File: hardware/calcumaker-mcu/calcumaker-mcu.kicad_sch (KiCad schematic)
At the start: 0 parts

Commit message: Checkpoint
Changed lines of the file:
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@@
 	)
 	(sheet
-		(at 320.04 40.64)
-		(size 36 22)
-		(exclude_from_sim no)
-		(in_bom yes)
-		(on_board yes)
-		(dnp no)
+		(at 40.64 40.64)
+		(size 36.00 22.00)
 		(fields_autoplaced yes)
-		(stroke
-			(width 0.1524)
-			(type solid)
+		(stroke (width 0.1524) (type solid))
+		(fill (color 0 0 0 0.0000))
+		(property "Sheetname" "MCU"
+			(at 40.64 39.37 0)
+			(effects (font (size 1.27 1.27)) (justify left bottom))
 		)
-		(fill
-			(color 0 0 0 0)
-		)
-		(property "Sheetname" "KeyboardIF"
-			(at 320.04 39.37 0)
-			(show_name no)
-			(do_not_autoplace no)
-			(effects
-				(font
-					(size 1.27 1.27)
-				)
-				(justify left bottom)
-			)
-		)
-		(property "Sheetfile" "keyboard_if.kicad_sch"
-			(at 320.04 63.91 0)
-			(show_name no)
-			(do_not_autoplace no)
-			(effects
-				(font
-					(size 1.27 1.27)
-				)
-				(justify left top)
-			)
+		(property "Sheetfile" "mcu.kicad_sch"
+			(at 40.64 63.91 0)
+			(effects (font (size 1.27 1.27)) (justify left top))
 		)
 	)
 	(sheet
-		(at 40.64 40.64)
-		(size 36 22)
-		(exclude_from_sim no)
-		(in_bom yes)
-		(on_board yes)
-		(dnp no)
+		(at 96.52 40.64)
+		(size 36.00 22.00)
 		(fields_autoplaced yes)
-		(stroke
-			(width 0.1524)
-			(type solid)
+		(stroke (width 0.1524) (type solid))
+		(fill (color 0 0 0 0.0000))
+		(property "Sheetname" "PSU"
+			(at 96.52 39.37 0)
+			(effects (font (size 1.27 1.27)) (justify left bottom))
 		)
-		(fill
-			(color 0 0 0 0)
-		)
-		(property "Sheetname" "MCU"
-			(at 40.64 39.37 0)
-			(show_name no)
-			(do_not_autoplace no)
-			(effects
-				(font
-					(size 1.27 1.27)
-				)
-				(justify left bottom)
-			)
-		)
-		(property "Sheetfile" "mcu.kicad_sch"
-			(at 40.64 63.91 0)
-			(show_name no)
-			(do_not_autoplace no)
-			(effects
-				(font
-					(size 1.27 1.27)
-				)
-				(justify left top)
-			)
+		(property "Sheetfile" "psu.kicad_sch"
+			(at 96.52 63.91 0)
+			(effects (font (size 1.27 1.27)) (justify left top))
 		)
 	)
 	(sheet
-		(at 375.92 40.64)
-		(size 36 22)
-		(exclude_from_sim no)
-		(in_bom yes)
-		(on_board yes)
-		(dnp no)
+		(at 152.40 40.64)
+		(size 36.00 22.00)
 		(fields_autoplaced yes)
-		(stroke
-			(width 0.1524)
-			(type solid)
+		(stroke (width 0.1524) (type solid))
+		(fill (color 0 0 0 0.0000))
+		(property "Sheetname" "KeyboardIF"
+			(at 152.40 39.37 0)
+			(effects (font (size 1.27 1.27)) (justify left bottom))
 		)
-		(fill
-			(color 0 0 0 0)
-		)
-		(property "Sheetname" "QSPIFlash"
-			(at 375.92 39.37 0)
-			(show_name no)
-			(do_not_autoplace no)
-			(effects
-				(font
-					(size 1.27 1.27)
-				)
-				(justify left bottom)
-			)
-		)
-		(property "Sheetfile" "qspi_flash.kicad_sch"
-			(at 375.92 63.91 0)
-			(show_name no)
-			(do_not_autoplace no)
-			(effects
-				(font
-					(size 1.27 1.27)
-				)
-				(justify left top)
-			)
+		(property "Sheetfile" "keyboard_if.kicad_sch"
+			(at 152.40 63.91 0)
+			(effects (font (size 1.27 1.27)) (justify left top))
 		)
 	)
 	(sheet
 		(at 208.28 40.64)
-		(size 36 22)
-		(exclude_from_sim no)
-		(in_bom yes)
-		(on_board yes)
-		(dnp no)
+		(size 36.00 22.00)
 		(fields_autoplaced yes)
-		(stroke
-			(width 0.1524)
-			(type solid)
+		(stroke (width 0.1524) (type solid))
+		(fill (color 0 0 0 0.0000))
+		(property "Sheetname" "QSPIFlash"
+			(at 208.28 39.37 0)
+			(effects (font (size 1.27 1.27)) (justify left bottom))
 		)
-		(fill
-			(color 0 0 0 0)
-		)
-		(property "Sheetname" "PSU"
-			(at 208.28 39.37 0)
-			(show_name no)
-			(do_not_autoplace no)
-			(effects
-				(font
-					(size 1.27 1.27)
-				)
-				(justify left bottom)
-			)
-		)
-		(property "Sheetfile" "psu.kicad_sch"
+		(property "Sheetfile" "qspi_flash.kicad_sch"
 			(at 208.28 63.91 0)
-			(show_name no)
-			(do_not_autoplace no)
-			(effects
-				(font
-					(size 1.27 1.27)
-				)
-				(justify left top)
-			)
+			(effects (font (size 1.27 1.27)) (justify left top))
 		)
 	)

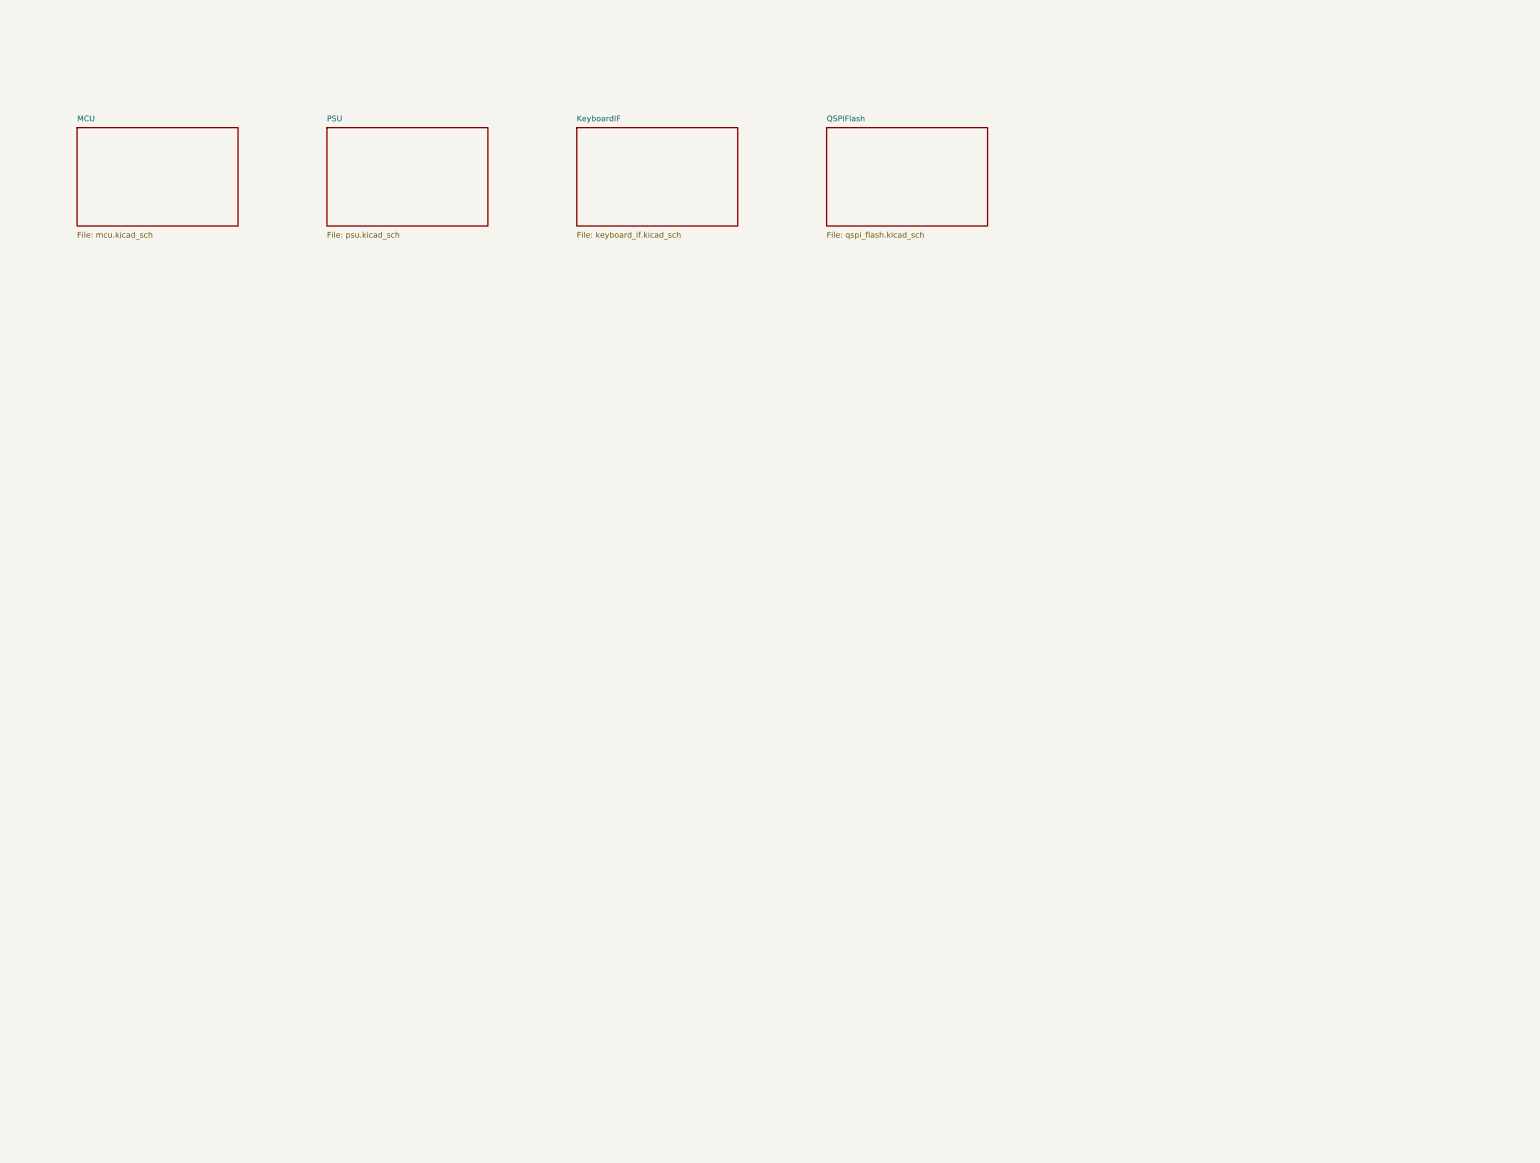
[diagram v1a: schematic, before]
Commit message: Wire mainboard and keypad schematics and verify expanded nets
Connect hierarchical interfaces, power/control circuits, debug links, matrix and RGB chains. Correct MCU package pins, diode polarity and power configuration; add bypass components and repeatable KiCad netlist/ERC checks. Document pin maps and remaining physical validation.
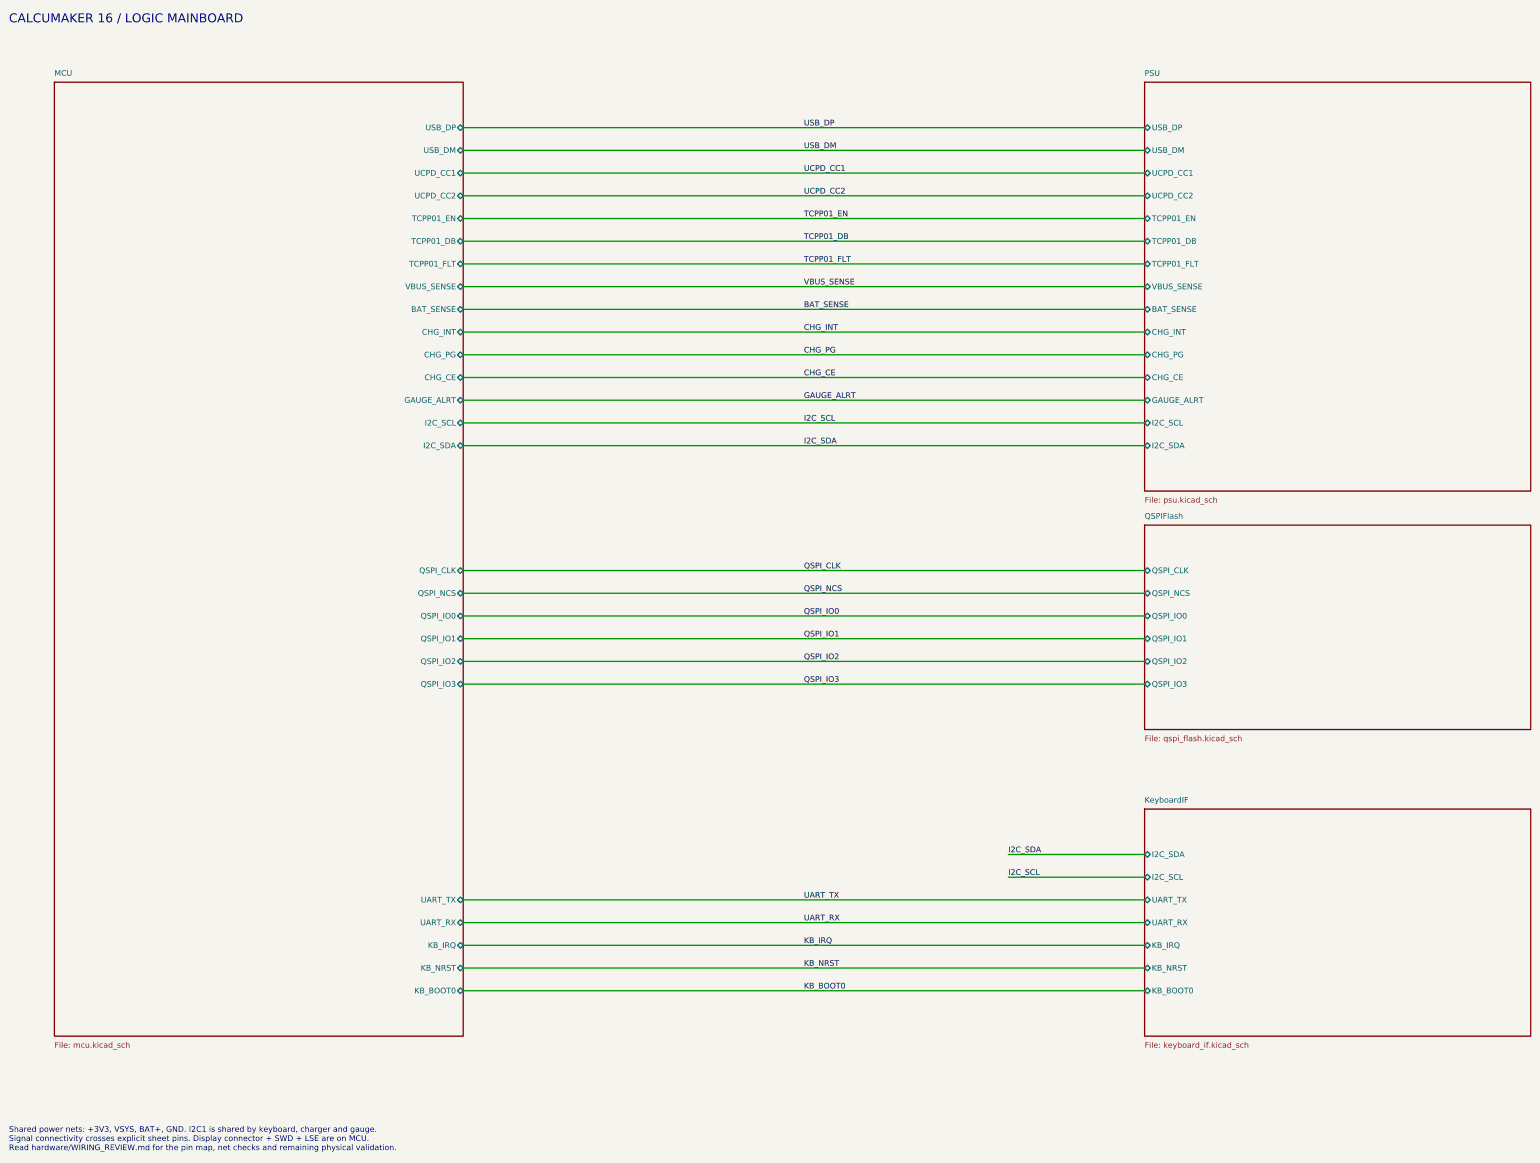
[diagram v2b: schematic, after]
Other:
- sheet KeyboardIF ports: added I2C_SCL, I2C_SDA, KB_BOOT0, KB_IRQ, KB_NRST, UART_RX, UART_TX; removed none
- sheet MCU ports: added BAT_SENSE, CHG_CE, CHG_INT, CHG_PG, GAUGE_ALRT, I2C_SCL, I2C_SDA, KB_BOOT0, KB_IRQ, KB_NRST, QSPI_CLK, QSPI_IO0, QSPI_IO1, QSPI_IO2, QSPI_IO3, QSPI_NCS, TCPP01_DB, TCPP01_EN, TCPP01_FLT, UART_RX, UART_TX, UCPD_CC1, UCPD_CC2, USB_DM, USB_DP, VBUS_SENSE; removed none
- sheet PSU ports: added BAT_SENSE, CHG_CE, CHG_INT, CHG_PG, GAUGE_ALRT, I2C_SCL, I2C_SDA, TCPP01_DB, TCPP01_EN, TCPP01_FLT, UCPD_CC1, UCPD_CC2, USB_DM, USB_DP, VBUS_SENSE; removed none
- sheet QSPIFlash ports: added QSPI_CLK, QSPI_IO0, QSPI_IO1, QSPI_IO2, QSPI_IO3, QSPI_NCS; removed none
- note added: "CALCUMAKER 16 / LOGIC MAINBOARD"
- note added: "Shared power nets: +3V3, VSYS, BAT+, GND. I2C1 is shared by keyboard, charger and gauge. Signal connectivity crosses explicit sheet pins. Display connector + SWD + LSE are on MCU. Read hardware/WIRING_REVIEW.md for the pin map, net checks and remaining physical validation."
- title: Calcumaker 16 — MCU -> Calcumaker 16 / mcu / calcumaker-mcu
